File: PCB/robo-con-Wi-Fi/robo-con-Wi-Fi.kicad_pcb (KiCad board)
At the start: 4 copper layers, 86 x 67 mm, 125 parts, among them J1 Conn_01x04, J2 SMA-J, J3 Conn_01x05, J4 Conn_01x01, J5 Conn_01x02, J6 Conn_01x01, J7 Conn_01x06, Q1 2SC3325-Y, SW1 SW_Push, SW2 SW_Push, U1 STM32H723VGTx, U10 MCP73831-2-OT, U11 LM66100DCK, U12 NJM12877, U13 TXB0606DYYR, U14 TPS628513DRLR, U15 LM66100DCK, U18 USB_Type-C, U2 LBEE5HY2FY, U3 TXU0204, U5 RKJXV122400R, U6 IS25LP064D-JLLE, U7 RKJXV122400R, U8 TMHU28, U9 TMHU28, Y2 XRCGB25M000FFS1AR0

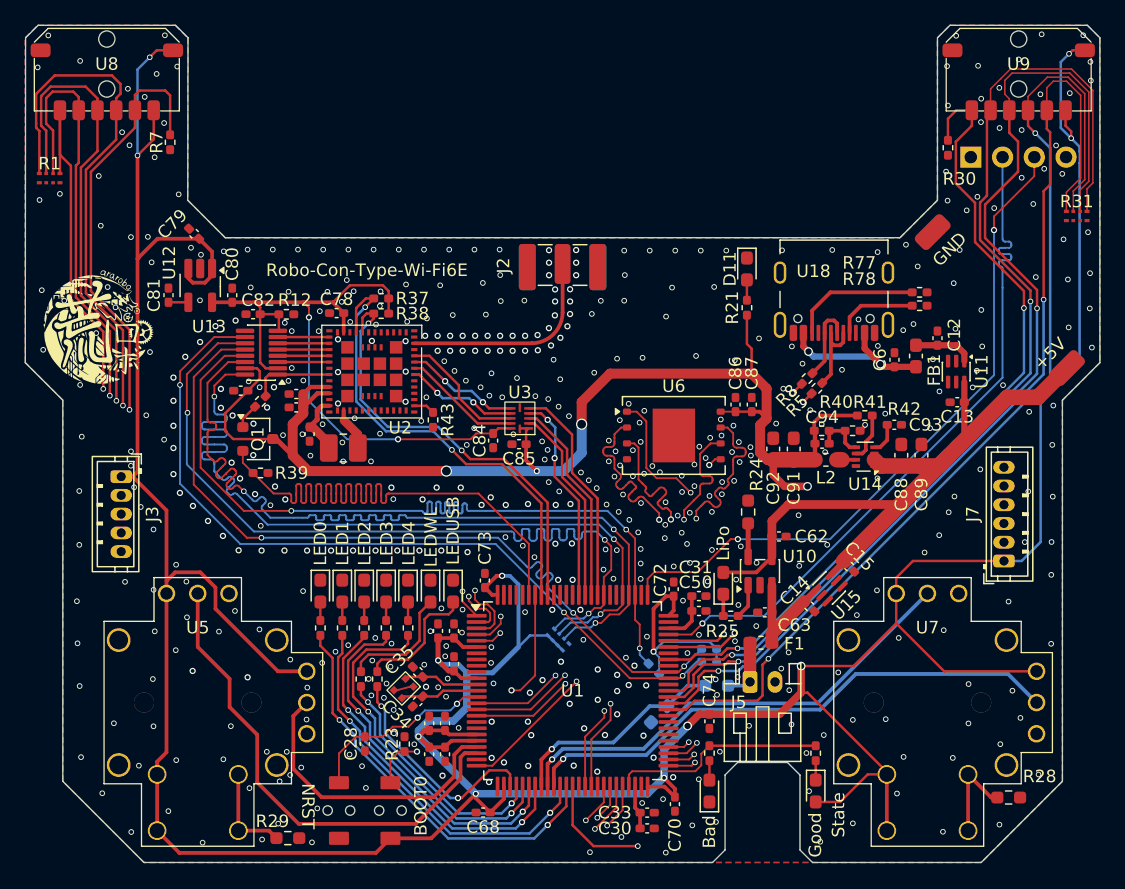
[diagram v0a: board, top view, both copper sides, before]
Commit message: M2穴追加
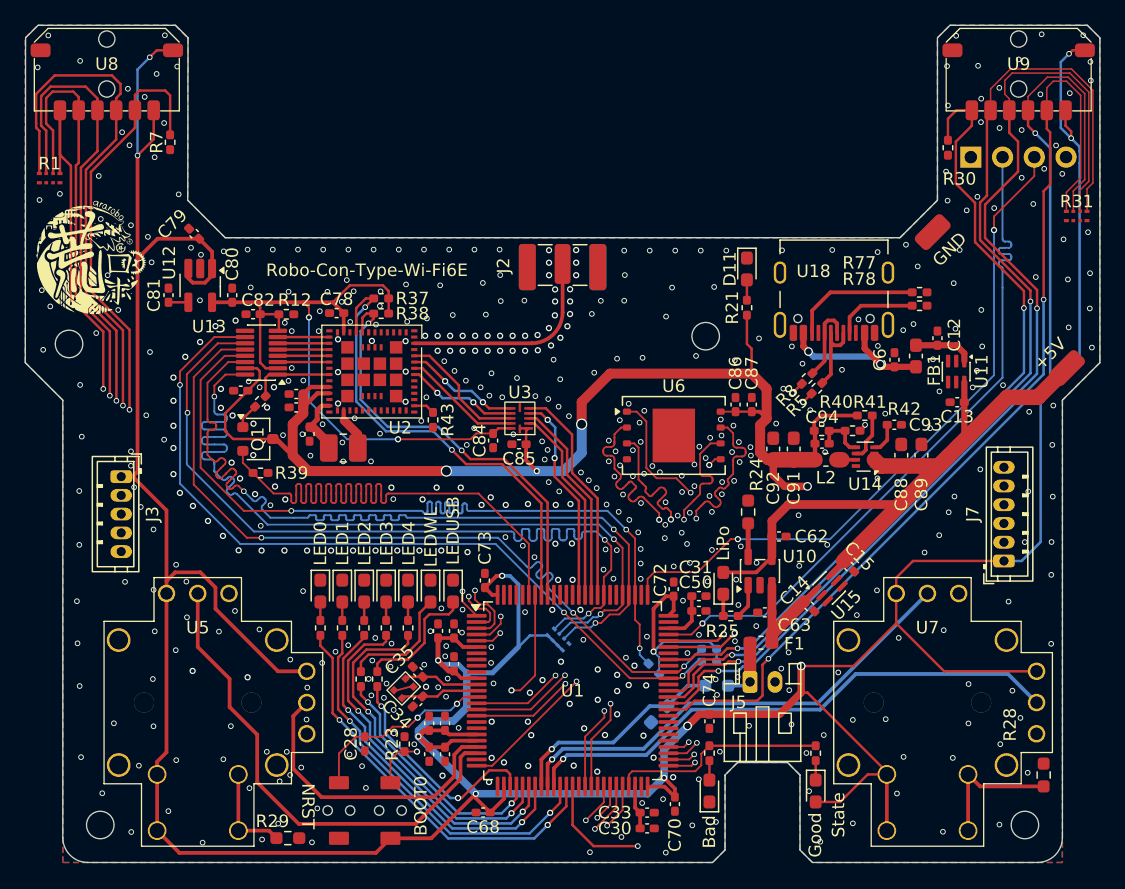
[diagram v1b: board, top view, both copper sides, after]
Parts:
- added REF**: MountingHole_2.2mm_M2, MountingHole:MountingHole_2.2mm_M2, F.Cu at (181.4, 47.9)
- added REF**: MountingHole_2.2mm_M2, MountingHole:MountingHole_2.2mm_M2, F.Cu at (207.0, 87.0)
- added REF**: MountingHole_2.2mm_M2, MountingHole:MountingHole_2.2mm_M2, F.Cu at (133.0, 87.0)
- added REF**: MountingHole_2.2mm_M2, MountingHole:MountingHole_2.2mm_M2, F.Cu at (130.5, 48.5)
- moved G*** 5.60 mm to (132.0, 42.0)
- moved R28 3.33 mm to (208.5, 83.0), turned to 90 degrees
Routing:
- net Right_Push_Stick: track 54.4 -> 57.7 mm
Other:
- outline, holes or cut-outs redrawn

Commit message: pcb
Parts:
- removed REF** (x4): MountingHole_2.2mm_M2, MountingHole:MountingHole_2.2mm_M2
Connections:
- U1 pad 15: SPI1_MOSI/QSPI1_IO0 -> unconnected-(U1-PC0-Pad15)
- U1 pad 16: SPI1_MISO/QSPI1_IO1 -> SPI1_MOSI/QSPI1_IO0
- U1 pad 17: WP/QSPI1_IO2 -> SPI1_MISO/QSPI1_IO1
- U1 pad 18: unconnected-(U1-PC3_C-Pad18) -> WP/QSPI1_IO2
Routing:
- net GND: vias 531 -> 533
